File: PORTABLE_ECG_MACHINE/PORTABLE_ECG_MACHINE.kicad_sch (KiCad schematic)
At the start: 73 parts, among them IC1 AD8232ACPZ, J1 UART, J2 AudioJack3, J3 Li-Ion 3.7 CONN, J4 USB_C_Receptacle_USB2.0, Q1 BSS138, Q2 BSS138, SW1 SW_SPDT, U1 SSD1306, U2 CP2102-GM, U3 TC1262-33, U4 TP4056

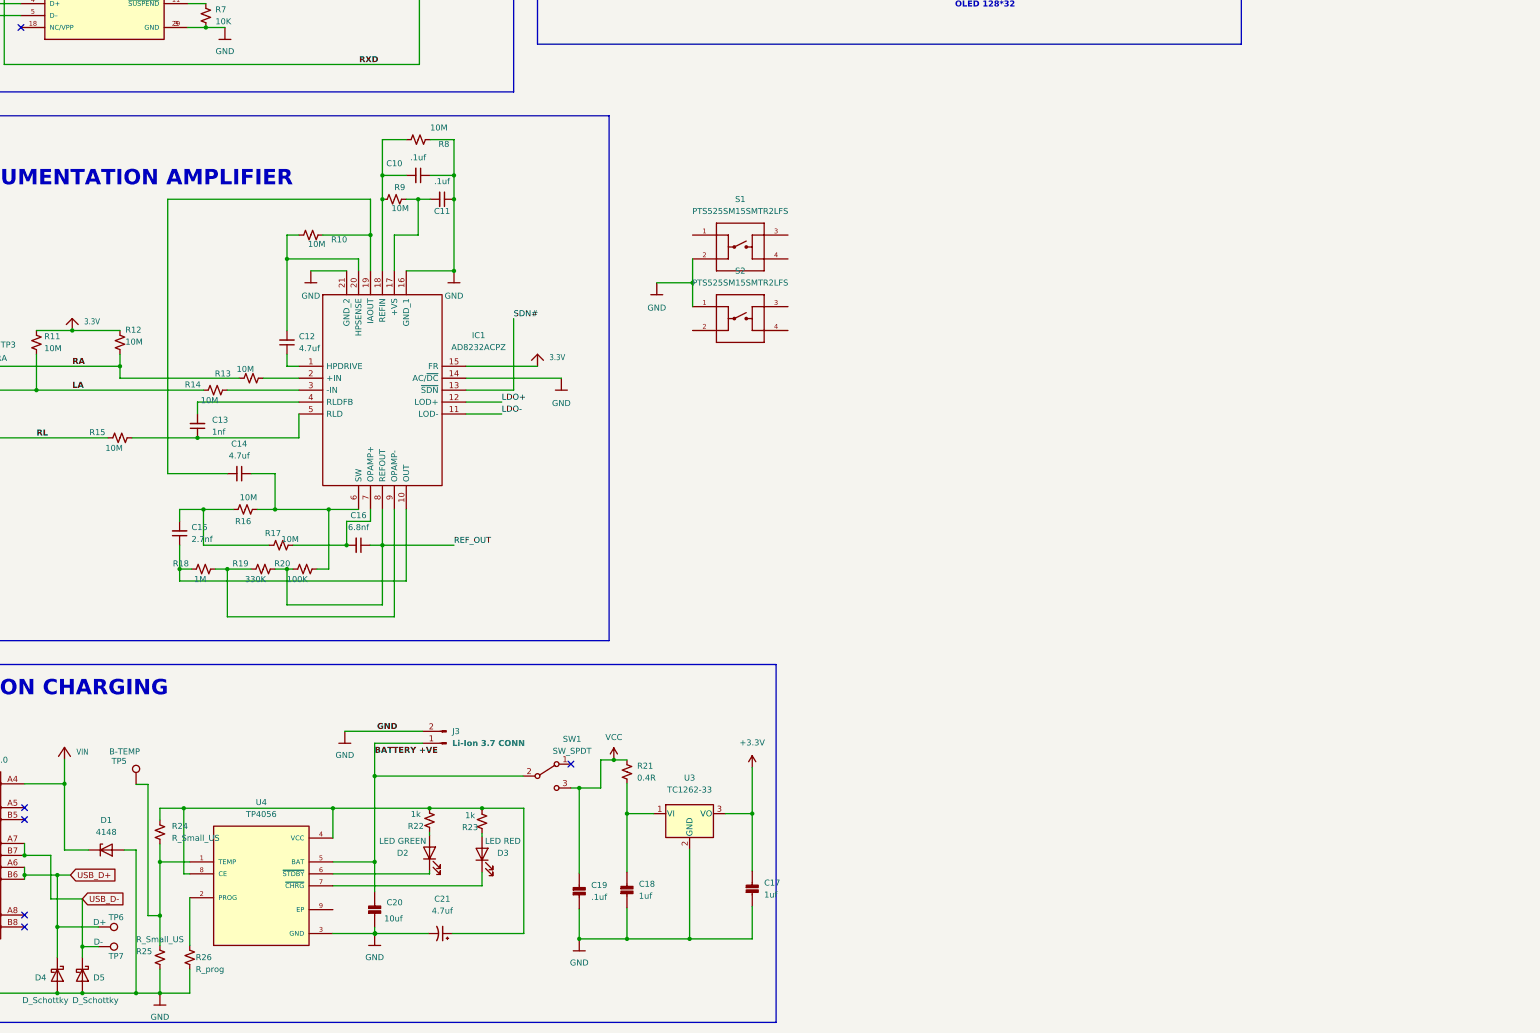
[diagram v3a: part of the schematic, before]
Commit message: OLED 3D change | uC add | .step gen v4
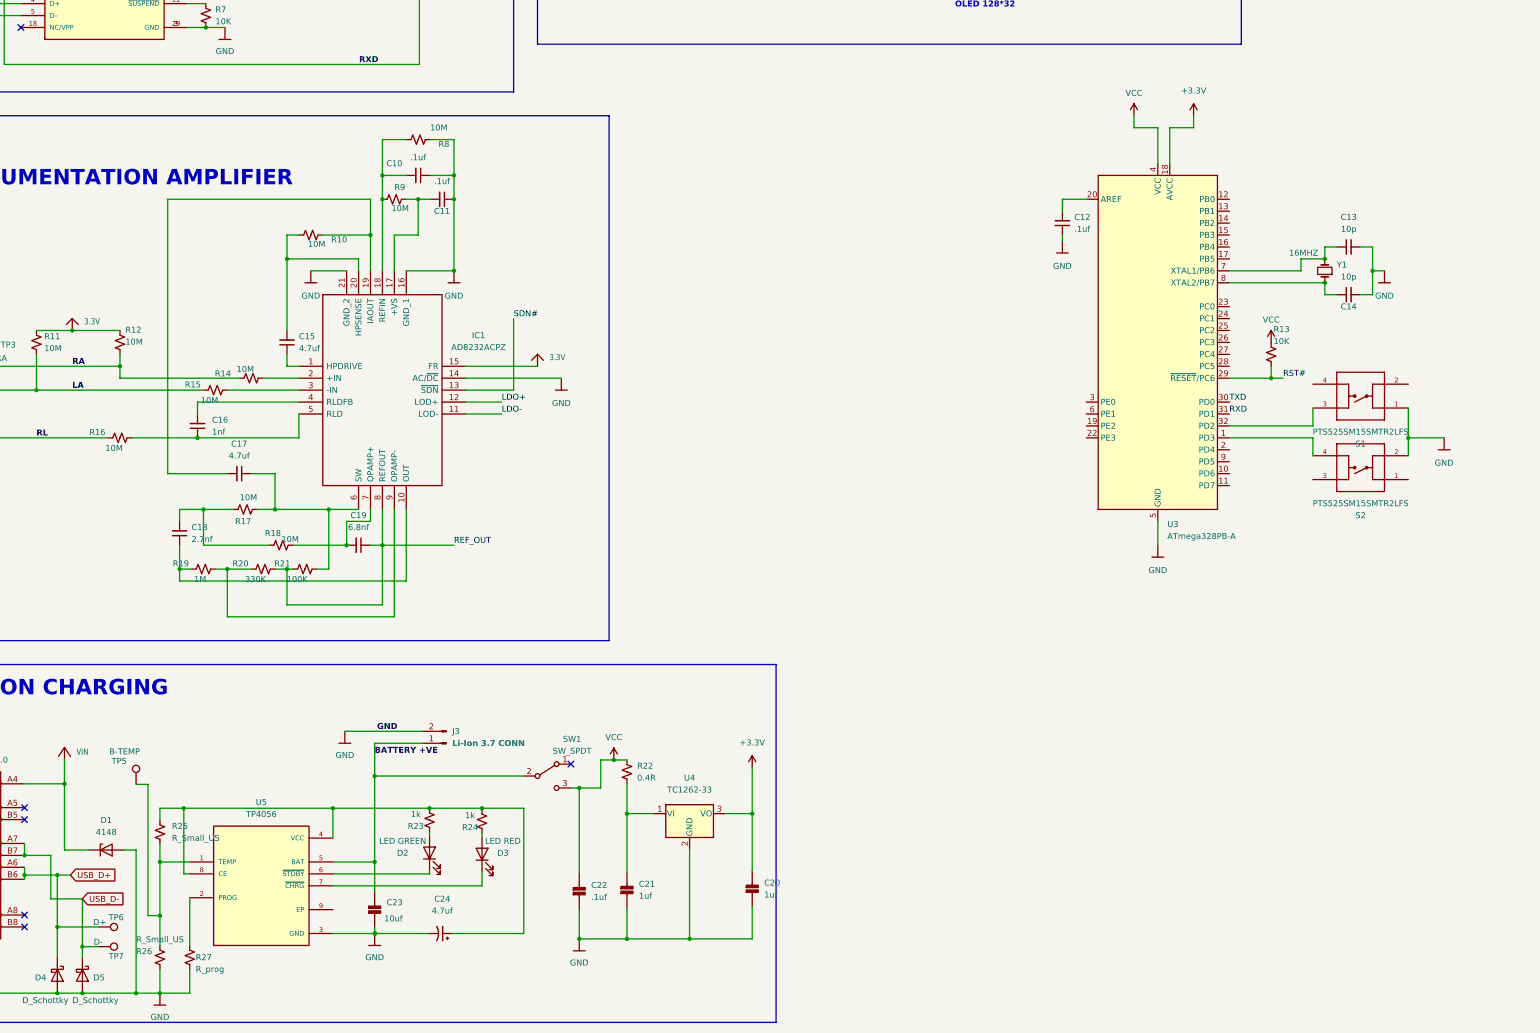
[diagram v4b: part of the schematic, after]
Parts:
- added C12: .1uf, Capacitor_SMD:C_0603_1608Metric, symbol Device:C_Small
- added C13: 10p, Capacitor_SMD:C_0603_1608Metric, symbol Device:C_Small
- added C14: 10p, Crystal:Crystal_SMD_2012-2Pin_2.0x1.2mm, symbol Device:C_Small
- added R13: 10K, Resistor_SMD:R_0603_1608Metric, symbol Device:R_Small_US
- added U3: ATmega328PB-A, Package_QFP:TQFP-32_7x7mm_P0.8mm, symbol MCU_Microchip_ATmega:ATmega328PB-A
- added Y1: 16MHZ, Crystal:Crystal_SMD_0603-2Pin_6.0x3.5mm, symbol Device:Crystal_Small
- renumbered C12 to C15, C13 to C16, C14 to C17, C15 to C18, C16 to C19, C17 to C20, C18 to C21, C19 to C22, C20 to C23, C21 to C24, R13 to R14, R14 to R15, R15 to R16, R16 to R17, R17 to R18, R18 to R19, R19 to R20, R20 to R21, R21 to R22, R22 to R23, R23 to R24, R24 to R25, R25 to R26, R26 to R27, S2 to S1, S1 to S2, U3 to U4, U4 to U5
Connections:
- net +3V3: now also U3.18 (AVCC)
- net GND: now also C12.1, C13.2, C14.2, U3.21 (GND), U3.5 (GND)
- net RXD: now also U3.31 (PD1)
- net TXD: now also U3.30 (PD0)
- net VCC: now also R13.1, U3.4 (VCC)
- net at S1.3: now also U3.32 (PD2)
- net at S2.4: now also U3.1 (PD3)
- new net: C12.2, U3.20 (AREF)
- new net: C13.1, U3.7 (XTAL1/PB6), Y1.2
- new net: C14.1, U3.8 (XTAL2/PB7), Y1.1
- new net RST#: R13.2, U3.29 (~{RESET}/PC6)
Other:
- moved on the sheet: S1, S2

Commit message: Conn complete | DRC CHECK2 | TEST INITIATE #V6#
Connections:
- net at S1.3: now also U3.26 (PC3); no longer U3.32 (PD2)
- net at U3.1 (PD3): no longer S2.4
- net at U3.11 (PD7): now also S2.3
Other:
- moved on the sheet: R13
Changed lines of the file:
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@@
+    (stroke (width 0) (type default) (color 0 0 0 0))
+  )
+  (wire (pts (xy 311.15 137.16) (xy 311.15 148.59))
     (stroke (width 0) (type default) (color 0 0 0 0))
   )
@@
     (stroke (width 0) (type default) (color 0 0 0 0))
   )
+  (wire (pts (xy 311.15 148.59) (xy 314.96 148.59))
+    (stroke (width 0) (type default) (color 0 0 0 0))
+  )
   (wire (pts (xy 132.08 119.38) (xy 132.08 104.14))
     (stroke (width 0) (type default) (color 0 0 0 0))
@@
     (stroke (width 0) (type default) (color 0 0 0 0))
   )
+  (wire (pts (xy 302.26 165.1) (xy 302.26 161.29))
+    (stroke (width 0) (type default) (color 0 0 0 0))
+  )
   (wire (pts (xy 96.52 182.88) (xy 96.52 190.5))
     (stroke (width 0) (type default) (color 0 0 0 0))
@@
     (stroke (width 0) (type default) (color 0 0 0 0))
   )
-  (wire (pts (xy 314.96 154.94) (xy 314.96 158.75))
-    (stroke (width 0) (type default) (color 0 0 0 0))
-  )
   (wire (pts (xy 75.438 39.624) (xy 97.028 39.624))
     (stroke (width 0) (type default) (color 0 0 0 0))
@@
     (stroke (width 0) (type default) (color 0 0 0 0))
   )
+  (wire (pts (xy 302.26 134.62) (xy 302.26 137.16))
+    (stroke (width 0) (type default) (color 0 0 0 0))
+  )
   (wire (pts (xy 280.67 53.467) (xy 280.67 53.721))
     (stroke (width 0) (type default) (color 0 0 0 0))
@@
   )
   (wire (pts (xy 167.64 43.18) (xy 167.64 43.815))
+    (stroke (width 0) (type default) (color 0 0 0 0))
+  )
+  (wire (pts (xy 302.26 161.29) (xy 314.96 161.29))
     (stroke (width 0) (type default) (color 0 0 0 0))
   )
@@
     (stroke (width 0) (type default) (color 0 0 0 0))
   )
+  (wire (pts (xy 297.18 134.62) (xy 302.26 134.62))
+    (stroke (width 0) (type default) (color 0 0 0 0))
+  )
   (wire (pts (xy 255.27 36.195) (xy 255.27 39.116))
     (stroke (width 0) (type default) (color 0 0 0 0))
   )
-  (wire (pts (xy 306.07 139.7) (xy 306.07 142.24))
-    (stroke (width 0) (type default) (color 0 0 0 0))
-  )
   (wire (pts (xy 122.682 33.782) (xy 122.682 49.784))
     (stroke (width 0) (type default) (color 0 0 0 0))
@@
     (stroke (width 0) (type default) (color 0 0 0 0))
   )
-  (wire (pts (xy 297.18 152.4) (xy 314.96 152.4))
-    (stroke (width 0) (type default) (color 0 0 0 0))
-  )
   (wire (pts (xy 79.248 67.564) (xy 83.312 67.564))
     (stroke (width 0) (type default) (color 0 0 0 0))
@@
     (stroke (width 0) (type default) (color 0 0 0 0))
   )
+  (wire (pts (xy 314.96 161.29) (xy 314.96 163.83))
+    (stroke (width 0) (type default) (color 0 0 0 0))
+  )
   (wire (pts (xy 25.4 266.7) (xy 25.4 273.177))
     (stroke (width 0) (type default) (color 0 0 0 0))
@@
     (stroke (width 0) (type default) (color 0 0 0 0))
   )
+  (wire (pts (xy 302.26 137.16) (xy 311.15 137.16))
+    (stroke (width 0) (type default) (color 0 0 0 0))
+  )
   (wire (pts (xy 240.03 39.116) (xy 240.03 48.641))
     (stroke (width 0) (type default) (color 0 0 0 0))
@@
     (stroke (width 0) (type default) (color 0 0 0 0))
   )
-  (wire (pts (xy 314.96 152.4) (xy 314.96 148.59))
-    (stroke (width 0) (type default) (color 0 0 0 0))
-  )
   (wire (pts (xy 130.302 36.322) (xy 124.714 36.322))
     (stroke (width 0) (type default) (color 0 0 0 0))
@@
     (stroke (width 0) (type default) (color 0 0 0 0))
   )
+  (wire (pts (xy 297.18 165.1) (xy 302.26 165.1))
+    (stroke (width 0) (type default) (color 0 0 0 0))
+  )
   (wire (pts (xy 168.91 228.6) (xy 168.91 234.95))
     (stroke (width 0) (type default) (color 0 0 0 0))
@@
     (stroke (width 0) (type default) (color 0 0 0 0))
   )
-  (wire (pts (xy 297.18 154.94) (xy 314.96 154.94))
-    (stroke (width 0) (type default) (color 0 0 0 0))
-  )
   (wire (pts (xy 106.299 233.807) (xy 106.299 240.157))
     (stroke (width 0) (type default) (color 0 0 0 0))
@@
   )
   (wire (pts (xy 78.74 170.18) (xy 73.66 170.18))
+    (stroke (width 0) (type default) (color 0 0 0 0))
+  )
+  (wire (pts (xy 306.07 133.35) (xy 306.07 142.24))
     (stroke (width 0) (type default) (color 0 0 0 0))
   )
@@
     (pin "2")
   )
-  (symbol (lib_id "Device:R_Small_US") (at 306.07 137.16 0) (unit 1)
+  (symbol (lib_id "Device:R_Small_US") (at 306.07 130.81 0) (unit 1)
     (in_bom yes) (on_board yes)
-    (property "Reference" "R13" (id 0) (at 306.578 131.826 0)
-      (effects (font (size 1.27 1.27)) (justify left))
-    )
-    (property "Value" "10K" (id 1) (at 306.578 134.366 0)
-      (effects (font (size 1.27 1.27)) (justify left))
-    )
-    (property "Footprint" "Resistor_SMD:R_0603_1608Metric" (id 2) (at 306.07 137.16 0)
-      (effects (font (size 1.27 1.27)) hide)
-    )
-    (property "Datasheet" "~" (id 3) (at 306.07 137.16 0)
+    (property "Reference" "R13" (id 0) (at 306.578 125.476 0)
+      (effects (font (size 1.27 1.27)) (justify left))
+    )
+    (property "Value" "10K" (id 1) (at 306.578 128.016 0)
+      (effects (font (size 1.27 1.27)) (justify left))
+    )
+    (property "Footprint" "Resistor_SMD:R_0603_1608Metric" (id 2) (at 306.07 130.81 0)
+      (effects (font (size 1.27 1.27)) hide)
+    )
+    (property "Datasheet" "~" (id 3) (at 306.07 130.81 0)
       (effects (font (size 1.27 1.27)) hide)
     )
@@
     (pin "2")
   )
-  (symbol (lib_id "power:VCC") (at 306.07 134.62 0) (unit 1)
-    (in_bom yes) (on_board yes) (fields_autoplaced)
-    (property "Reference" "#PWR04" (id 0) (at 306.07 138.43 0)
-      (effects (font (size 1.27 1.27)) hide)
-    )
-    (property "Value" "VCC" (id 1) (at 306.07 129.794 0))
-    (property "Footprint" "" (id 2) (at 306.07 134.62 0)
-      (effects (font (size 1.27 1.27)) hide)
-    )
-    (property "Datasheet" "" (id 3) (at 306.07 134.62 0)
-      (effects (font (size 1.27 1.27)) hide)
-    )
+  (symbol (lib_id "power:VCC") (at 306.07 128.27 0) (unit 1)
+    (in_bom yes) (on_board yes) (fields_autoplaced)
+    (property "Reference" "#PWR04" (id 0) (at 306.07 132.08 0)
+      (effects (font (size 1.27 1.27)) hide)
+    )
+    (property "Value" "VCC" (id 1) (at 306.07 123.444 0))
+    (property "Footprint" "" (id 2) (at 306.07 128.27 0)
+      (effects (font (size 1.27 1.27)) hide)
+    )
+    (property "Datasheet" "" (id 3) (at 306.07 128.27 0)
+      (effects (font (size 1.27 1.27)) hide)
+    )

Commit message: CUSTOM PAD ADD | ANNOTATION CONFLICT RECTIFY
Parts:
- added J5: Conn_01x06_Male, TEST_POINT_MATRIX_6-PIN:6PIN_CONN, symbol Connector:Conn_01x06_Male
- renumbered TP5 to B_TEMP1, TP6 to D+1, TP7 to D-1, D4 to D2, D5 to D3, S1 to DRIVE1, D2 to GREEN1, TP2 to LA1, R13 to R11, R11 to R12, R12 to R13, TP3 to RA1, D3 to RED1, TP4 to RL1, TP1 to RST_CP1, S2 to SELECT1
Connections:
- net at U3.12 (PB0): now also J5.6 (Pin_6)
- net at U3.13 (PB1): now also J5.5 (Pin_5)
- net at U3.14 (PB2): now also J5.4 (Pin_4)
- net at U3.15 (PB3): now also J5.3 (Pin_3)
- net at U3.16 (PB4): now also J5.2 (Pin_2)
- net at U3.17 (PB5): now also J5.1 (Pin_1)

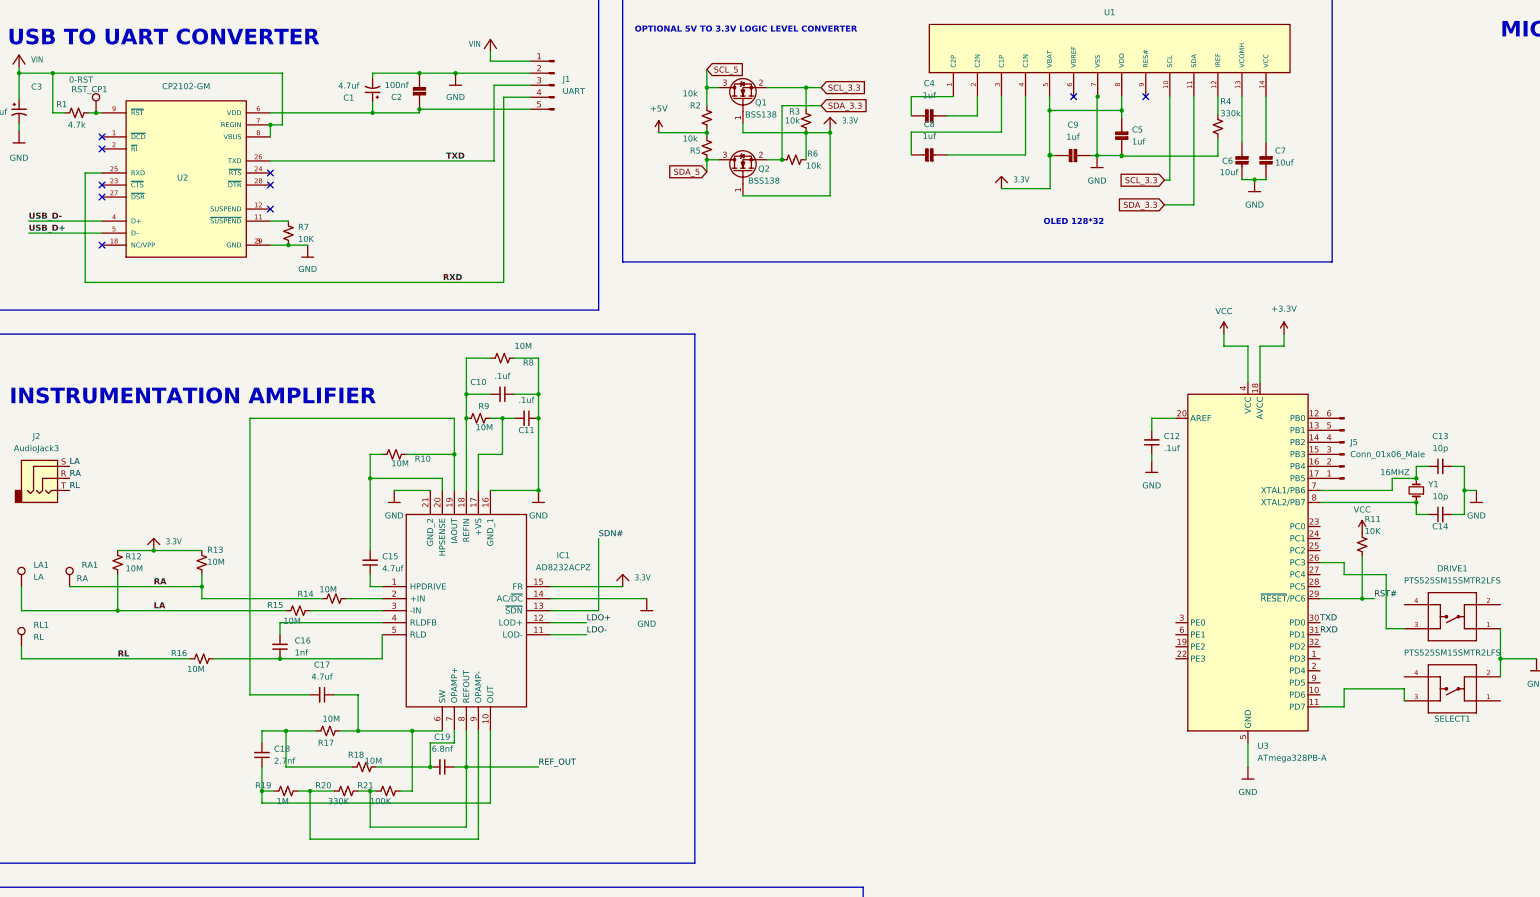
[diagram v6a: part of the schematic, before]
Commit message: conn complete | solder jumper add
pcbnew connection complete with respect to schematics, solder jumper add
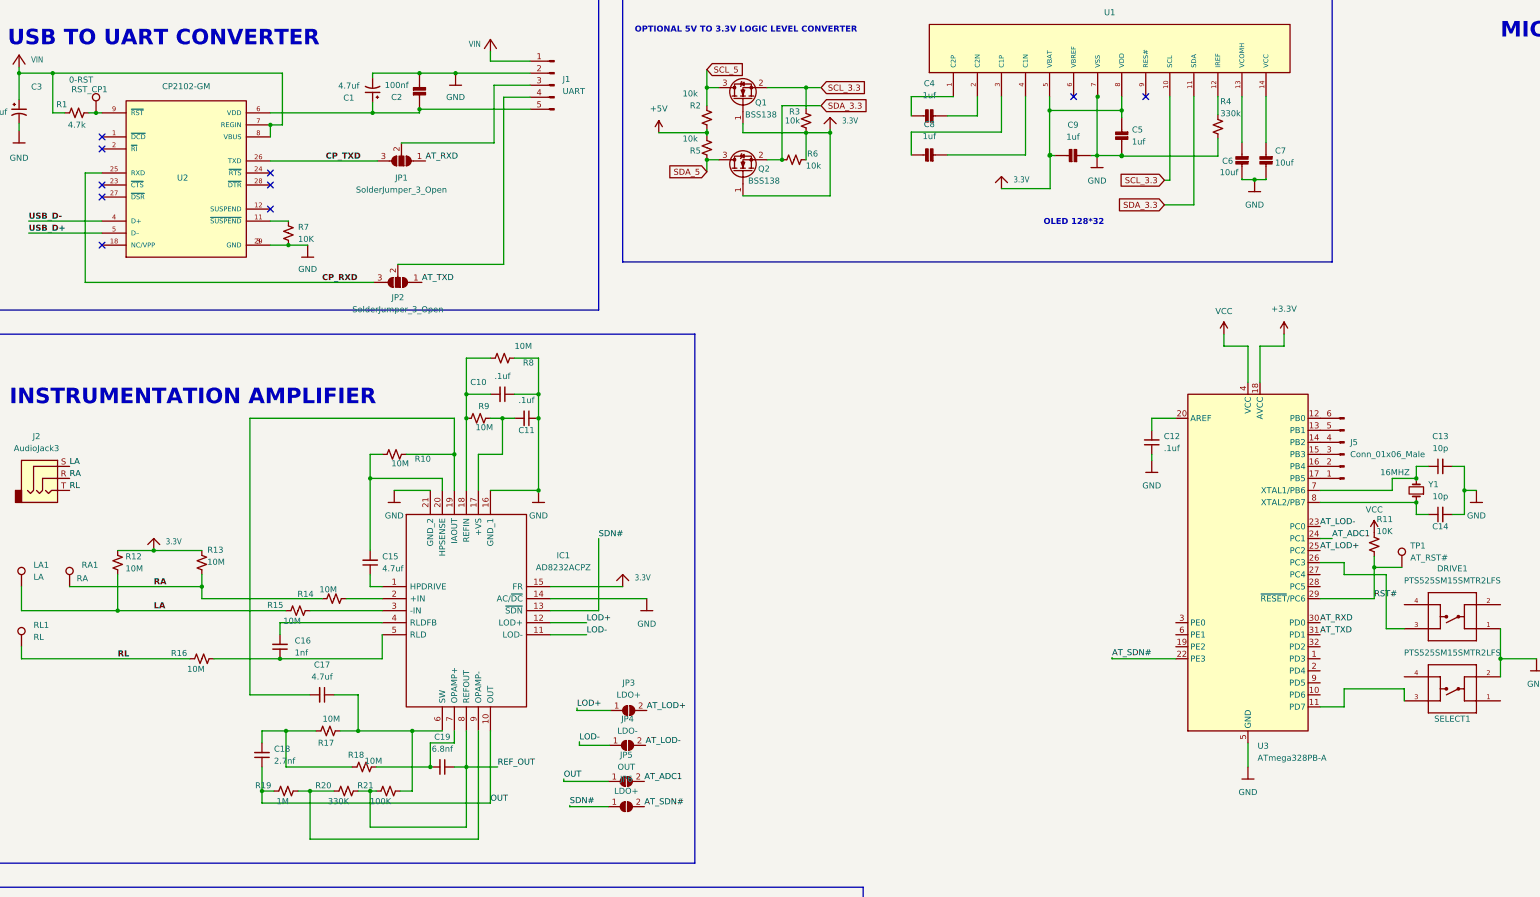
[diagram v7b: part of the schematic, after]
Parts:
- added JP1, JP2: SolderJumper_3_Open, TEST_POINT_MATRIX_6-PIN:3_PIN_SOLDER_JUMPER_SMD, symbol Jumper:SolderJumper_3_Open
- added JP3, JP6: LDO+, TEST_POINT_MATRIX_6-PIN:2_PIN_SMD_SOLDER_JUMPER, symbol Jumper:SolderJumper_2_Open
- added JP4: LDO-, TEST_POINT_MATRIX_6-PIN:2_PIN_SMD_SOLDER_JUMPER, symbol Jumper:SolderJumper_2_Open
- added JP5: OUT, TEST_POINT_MATRIX_6-PIN:2_PIN_SMD_SOLDER_JUMPER, symbol Jumper:SolderJumper_2_Open
- added TP1: AT_RST#, TestPoint:TestPoint_Pad_D1.0mm, symbol Connector:TestPoint
- DRIVE1, SELECT1: footprint SW_PTS525SM15SMTR2LFS -> tactile switch:SW_PTS525SM15SMTR2LFS
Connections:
- net RST#: now also TP1.1
- net SDN#: now also JP6.1 (A)
- net AT_SDN#: now reaches U3.22 (PE3)
- net AT_SDN#: now also JP6.2 (B)
- net AT_LOD-: now reaches U3.23 (PC0)
- net AT_LOD-: now also JP4.2 (B)
- net AT_ADC1: now reaches U3.24 (PC1)
- net AT_ADC1: now also JP5.2 (B)
- net AT_LOD+: now reaches U3.25 (PC2)
- net AT_LOD+: now also JP3.2 (B)
- net OUT: now reaches C18.1, IC1.10 (OUT), R19.1
- net OUT: now also JP5.1 (A)
- net LDO+ renamed LOD+
- net LOD+: now also JP3.1 (A)
- net LDO- renamed LOD-
- net LOD-: now also JP4.1 (A)
- removed net RXD: J1.4 (Pin_4), U2.25 (RXD), U3.31 (PD1)
- removed net TXD: J1.3 (Pin_3), U2.26 (TXD), U3.30 (PD0)
- new net: J1.3 (Pin_3), JP1.2 (C)
- new net: J1.4 (Pin_4), JP2.2 (C)
- new net AT_RXD: JP1.1 (A), U3.30 (PD0)
- new net AT_TXD: JP2.1 (A), U3.31 (PD1)
- new net CP_RXD: JP2.3 (B), U2.25 (RXD)
- new net CP_TXD: JP1.3 (B), U2.26 (TXD)
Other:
- moved on the sheet: R11
